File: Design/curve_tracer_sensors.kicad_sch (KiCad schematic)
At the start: 15 parts, among them U401 INA210, U402 OPA990

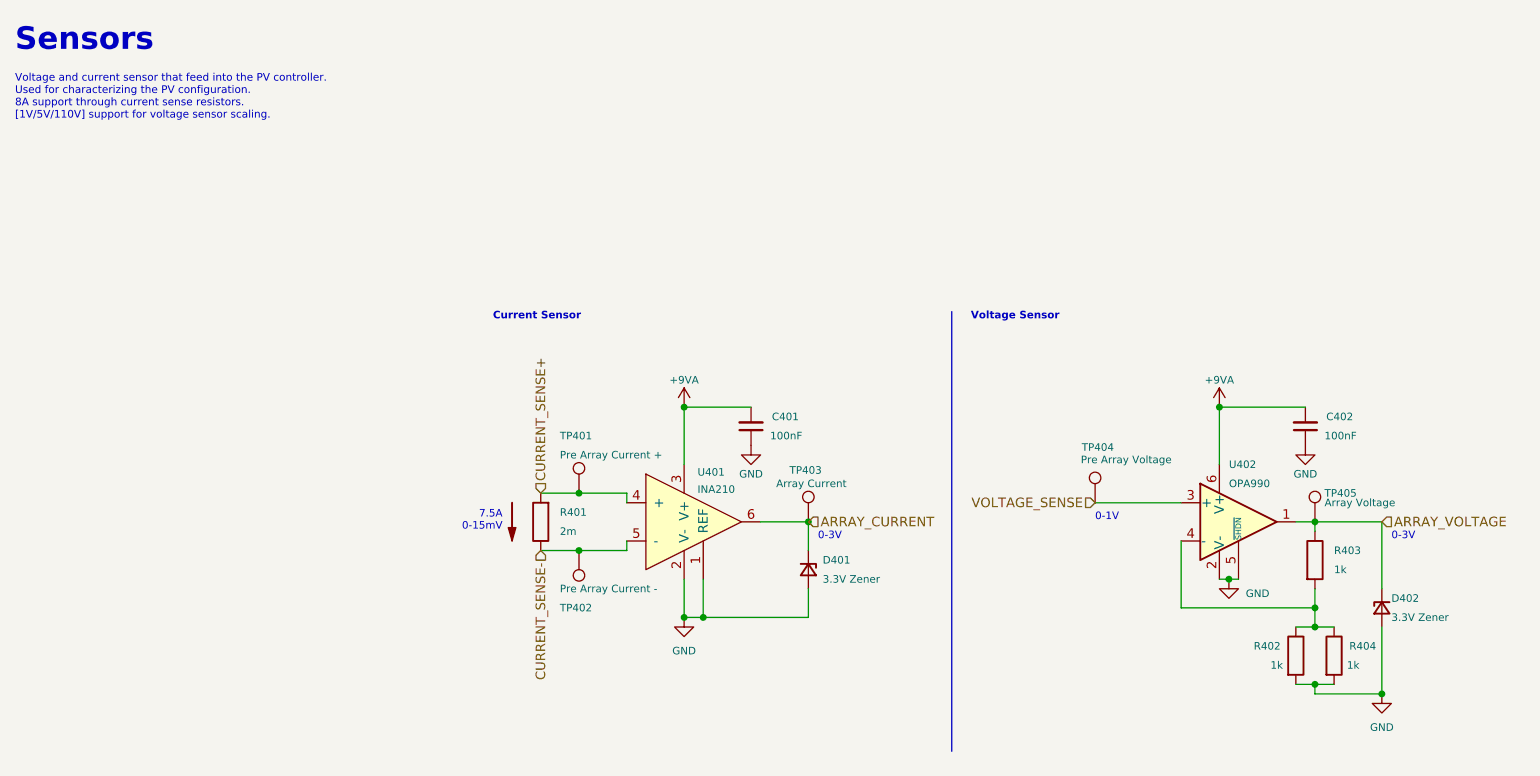
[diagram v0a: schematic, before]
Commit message: cleanup and fix errors for v1.3.0, proposed v1.4.0
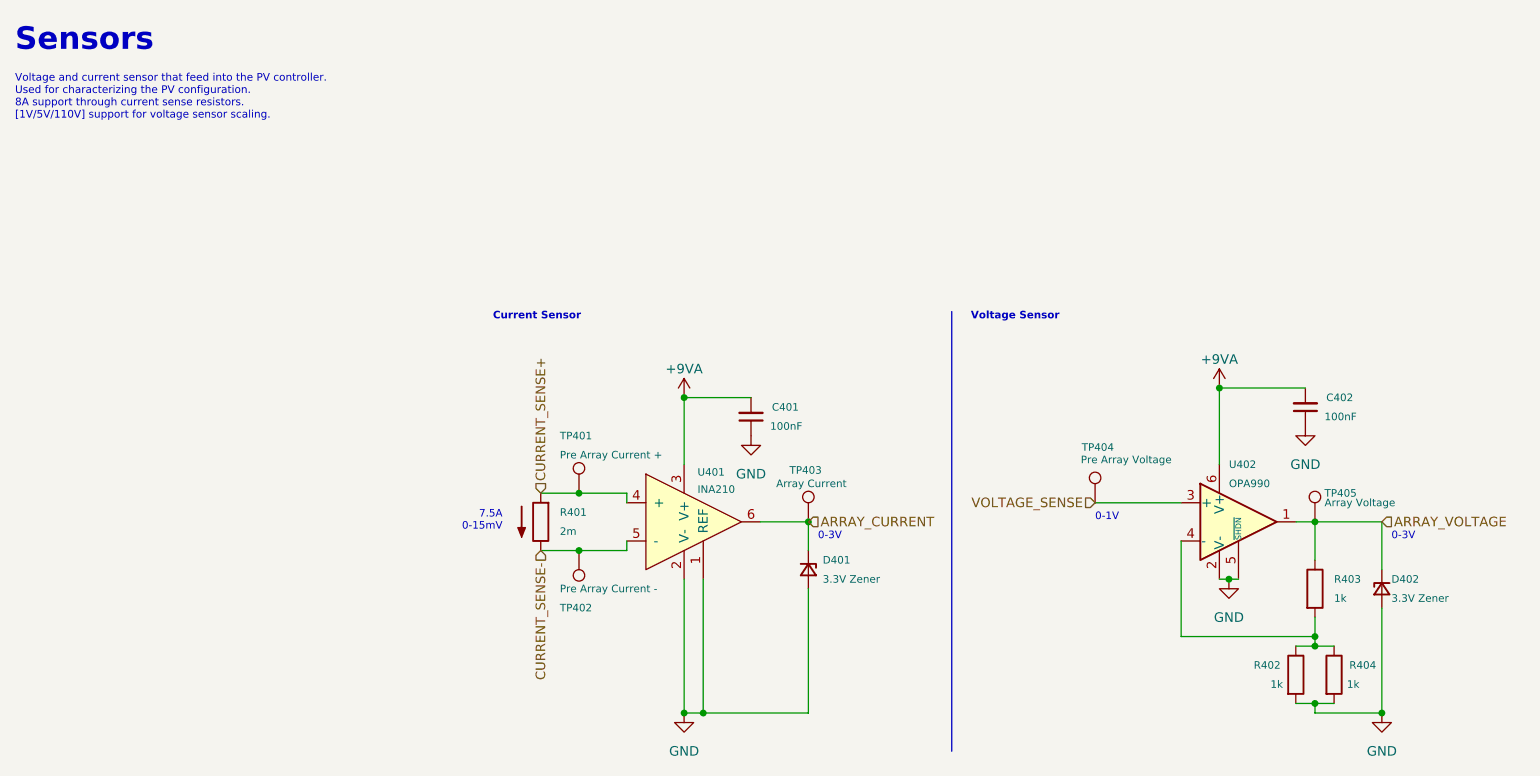
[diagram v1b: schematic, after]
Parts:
- C401, C402: Cost (none) -> 0.0078; JLCPCB BOM 1 -> (none); LCSC Part C28233 -> (none); LCSC Part # (none) -> C28233; P/N (none) -> CL21B104KCFNNNE; Part Number N/A -> (none); Projected Cost 0.0083 -> (none); Purchase Page N/A -> (none)
- D401, D402: Cost (none) -> 0.0108; JLCPCB BOM 1 -> (none); LCSC Part C8056 -> (none); LCSC Part # (none) -> C8056; P/N (none) -> ZMM3V3-M; Part Number N/A -> (none); Projected Cost 0.0205 -> (none); Purchase Page N/A -> (none)
- R401: Alternative Part https://www.mouser.com/ProductDetail/Bourns/CRF1206-FZ-R002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 -> (none); Cost (none) -> 0.73; JLCPCB BOM 0 -> (none); LCSC Part N/A -> (none); Manufacturer Part Number PMR18EZPFV2L00 -> (none); P/N (none) -> PMR18EZPFV2L00; Part Number 755-PMR18EZPFV2L00 -> (none); Projected Cost 0.69 -> (none); Purchase Page https://www.mouser.com/ProductDetail/ROHM-Semiconductor/PMR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 -> (none)
- R402, R403, R404: Cost (none) -> 0.0021; JLCPCB BOM 1 -> (none); LCSC Part C17513 -> (none); LCSC Part # (none) -> C17513; Manufacturer Uniroyal Elec -> UNI-ROYAL(Uniroyal Elec); P/N (none) -> 0805W8F1001T5E; Part Number N/A -> (none); Projected Cost 0.0021 -> (none); Purchase Page N/A -> (none)
- TP401, TP402, TP403, TP404, TP405: Part Number N/A -> (none)
- U401: Cost (none) -> 1.04; Distributor Texas Instruments -> Mouser; JLCPCB BOM 0 -> (none); LCSC Part N/A -> (none); P/N (none) -> INA210AIDCKT; Part Number INA210AIDCKT -> (none); Projected Cost 1.156 -> (none); Purchase Page https://www.ti.com/store/ti/en/p/product/?p=INA210AIDCKT&HQ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 -> (none)
- U402: Alternative Part OPA991, OPA992 -> (none); Cost (none) -> 1.31; JLCPCB BOM 0 -> (none); LCSC Part N/A -> (none); Manufacturer Part Number OPA990SIDBVR -> (none); Mouser Part 595-OPA990SIDBVR -> (none); P/N (none) -> OPA990SIDBVR; Part Number OPA990SIDBVR -> (none); Projected Cost 1.30 -> (none); Purchase Page https://www.mouser.com/ProductDetail/595-OPA990SIDBVR -> (none)
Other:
- moved on the sheet: C401, C402, D402, R402, R403, R404
